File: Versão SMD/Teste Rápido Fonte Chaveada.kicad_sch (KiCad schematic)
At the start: 16 parts, among them CN1 W4505-20PDRDTXR, SW1 SW_DPST_x2

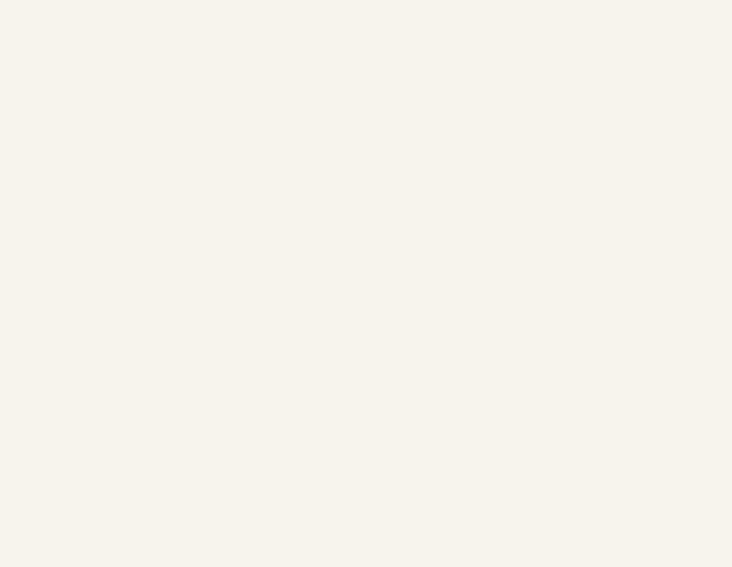
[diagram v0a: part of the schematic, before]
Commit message: Adicionado cargas de teste por Rail.
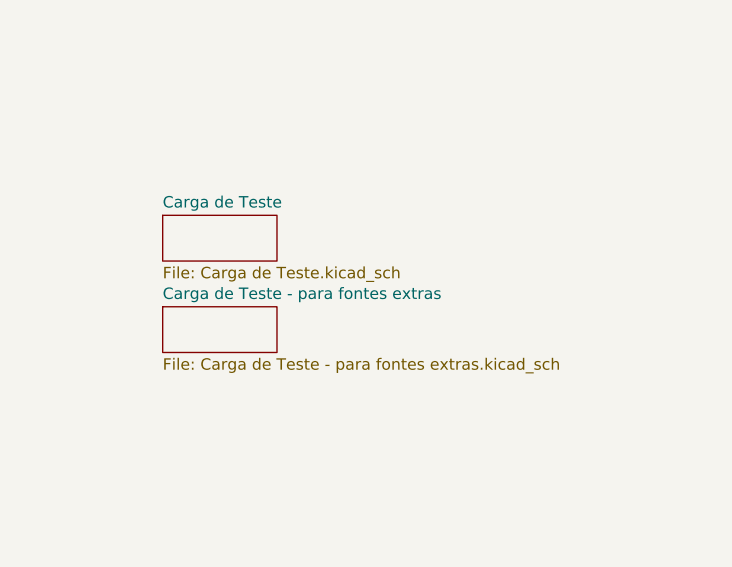
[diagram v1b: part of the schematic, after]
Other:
- added sheet Carga de Teste (Carga de Teste.kicad_sch)
- added sheet Carga de Teste - para fontes extras (Carga de Teste - para fontes extras.kicad_sch)
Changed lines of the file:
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@@
+		)
+	)
+	(sheet
+		(at 190.5 73.66)
+		(size 12.7 5.08)
+		(fields_autoplaced yes)
+		(stroke
+			(width 0.1524)
+			(type solid)
+		)
+		(fill
+			(color 0 0 0 0.0000)
+		)
+		(property "Sheetname" "Carga de Teste"
+			(at 190.5 72.9484 0)
+			(effects
+				(font
+					(size 1.27 1.27)
+				)
+				(justify left bottom)
+			)
+		)
+		(property "Sheetfile" "Carga de Teste.kicad_sch"
+			(at 190.5 79.3246 0)
+			(effects
+				(font
+					(size 1.27 1.27)
+				)
+				(justify left top)
+			)
+		)
+		(instances
+			(project "Teste Rápido Fonte Chaveada"
+				(path "/05a0489b-6f48-4980-a6d7-922522b33b13"
+					(page "2")
+				)
+			)
+		)
+	)
+	(sheet
+		(at 190.5 83.82)
+		(size 12.7 5.08)
+		(fields_autoplaced yes)
+		(stroke
+			(width 0.1524)
+			(type solid)
+		)
+		(fill
+			(color 0 0 0 0.0000)
+		)
+		(property "Sheetname" "Carga de Teste - para fontes extras"
+			(at 190.5 83.1084 0)
+			(effects
+				(font
+					(size 1.27 1.27)
+				)
+				(justify left bottom)
+			)
+		)
+		(property "Sheetfile" "Carga de Teste - para fontes extras.kicad_sch"
+			(at 190.5 89.4846 0)
+			(effects
+				(font
+					(size 1.27 1.27)
+				)
+				(justify left top)
+			)
+		)
+		(property "Campo2" ""
+			(at 190.5 83.82 0)
+			(effects
+				(font
+					(size 1.27 1.27)
+				)
+				(hide yes)
+			)
+		)
+		(instances
+			(project "Teste Rápido Fonte Chaveada"
+				(path "/05a0489b-6f48-4980-a6d7-922522b33b13"
+					(page "3")
+				)
+			)
 		)
 	)
